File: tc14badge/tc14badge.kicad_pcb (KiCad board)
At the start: 2 copper layers, 67 x 71 mm, 50 parts, among them J1 GSG-900MHZ-F-ANTENNA, J2 GSG-USB-MICRO-B, P1 EXPANSION, P2 ANTENNA, P3 RESET_N, P4 DD, P5 DC, P6 3V3, P7 GND, P8 GOODFET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

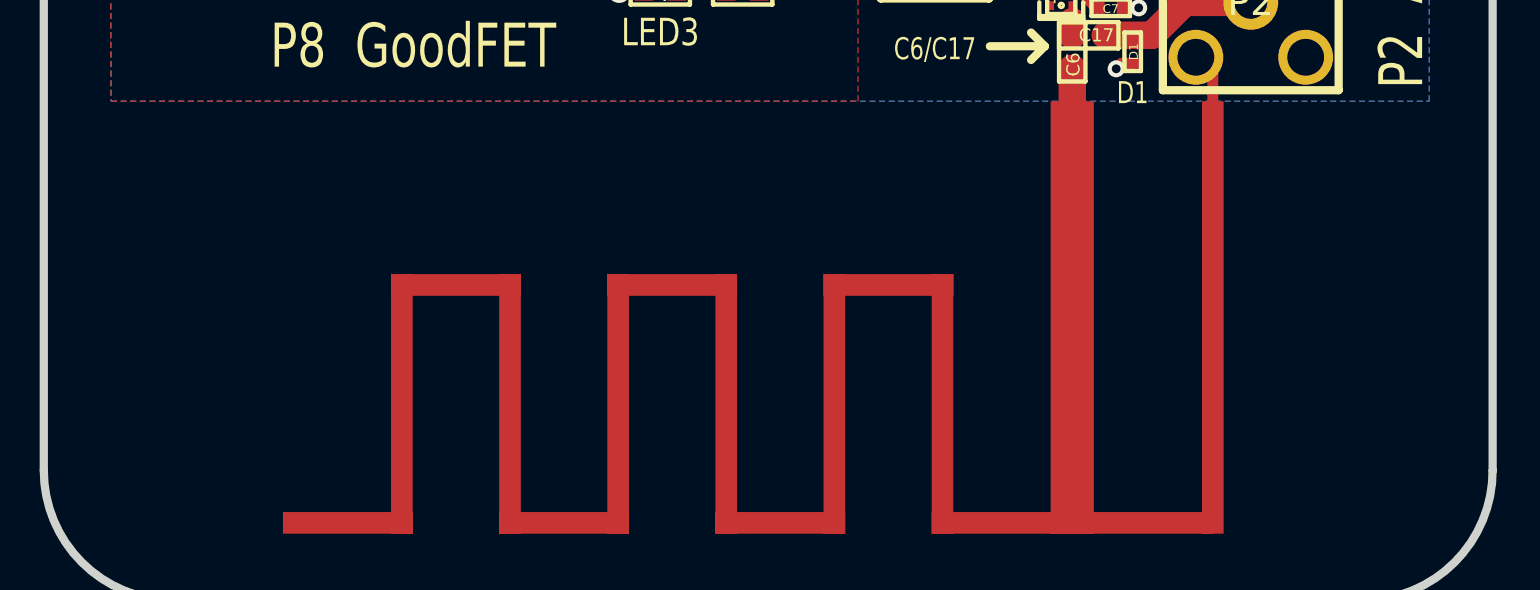
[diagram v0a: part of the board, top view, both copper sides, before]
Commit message: Added BSides and defcon icons to silkscreen + generated gerbers for prod run
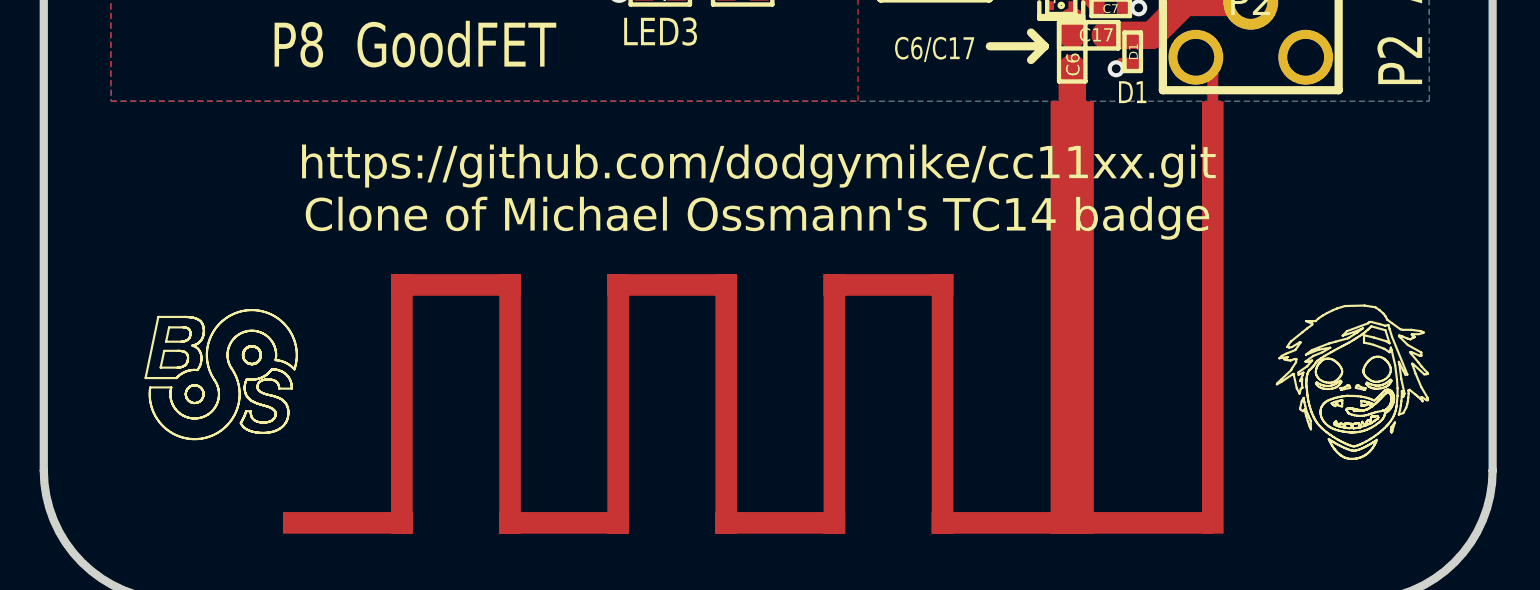
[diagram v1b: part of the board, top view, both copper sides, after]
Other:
- board text added: "https://github.com/dodgymike/cc11xx.git Clone of Michael Ossmann's TC14 badge"
